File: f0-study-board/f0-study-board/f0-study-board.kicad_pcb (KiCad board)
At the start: 4 copper layers, 47.8 x 19 mm, 26 parts, among them J1 PinHeader-18pin, J2 PinHeader-18pin, J3 USB_B_Micro, J4 SWD, SW1 SW_Reset, U1 STM32F091CBT6, U2 XC6206P332MR, Y1 8MHz

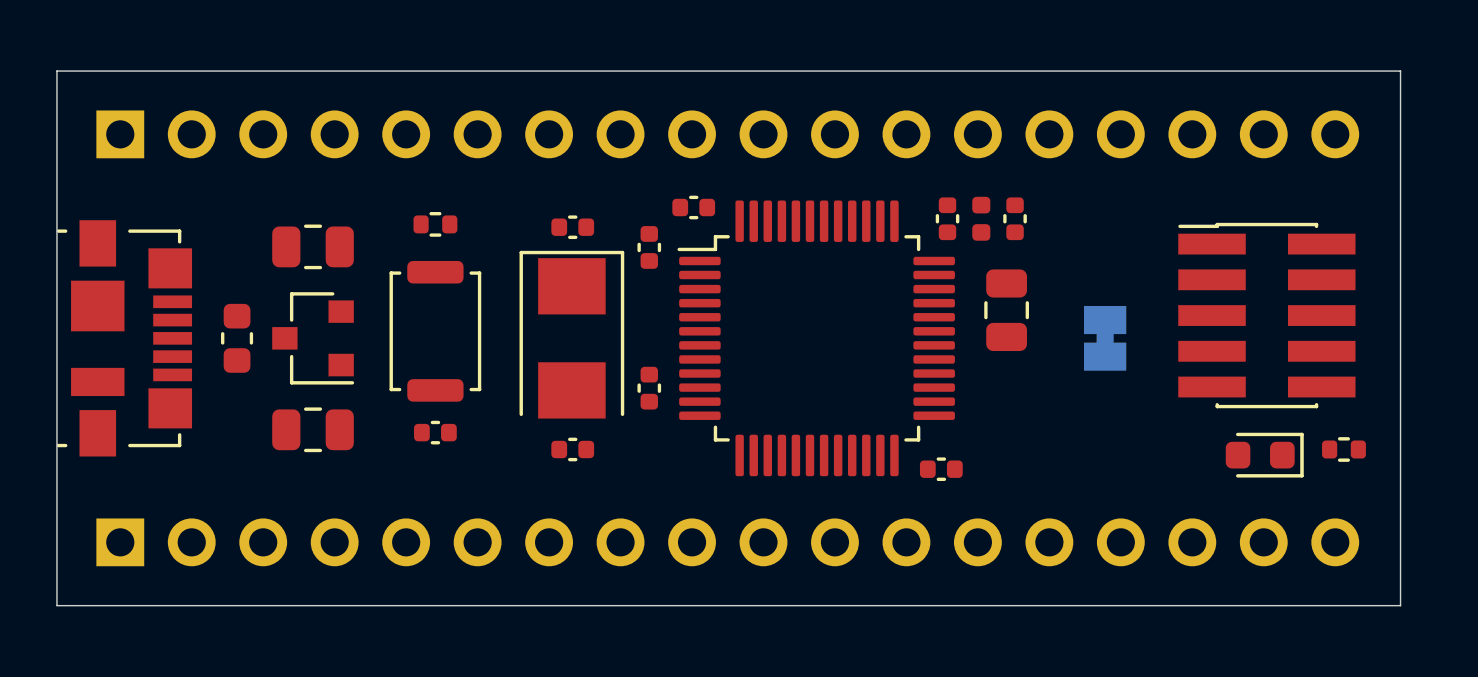
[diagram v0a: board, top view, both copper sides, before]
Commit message: Routed the board, ready for export
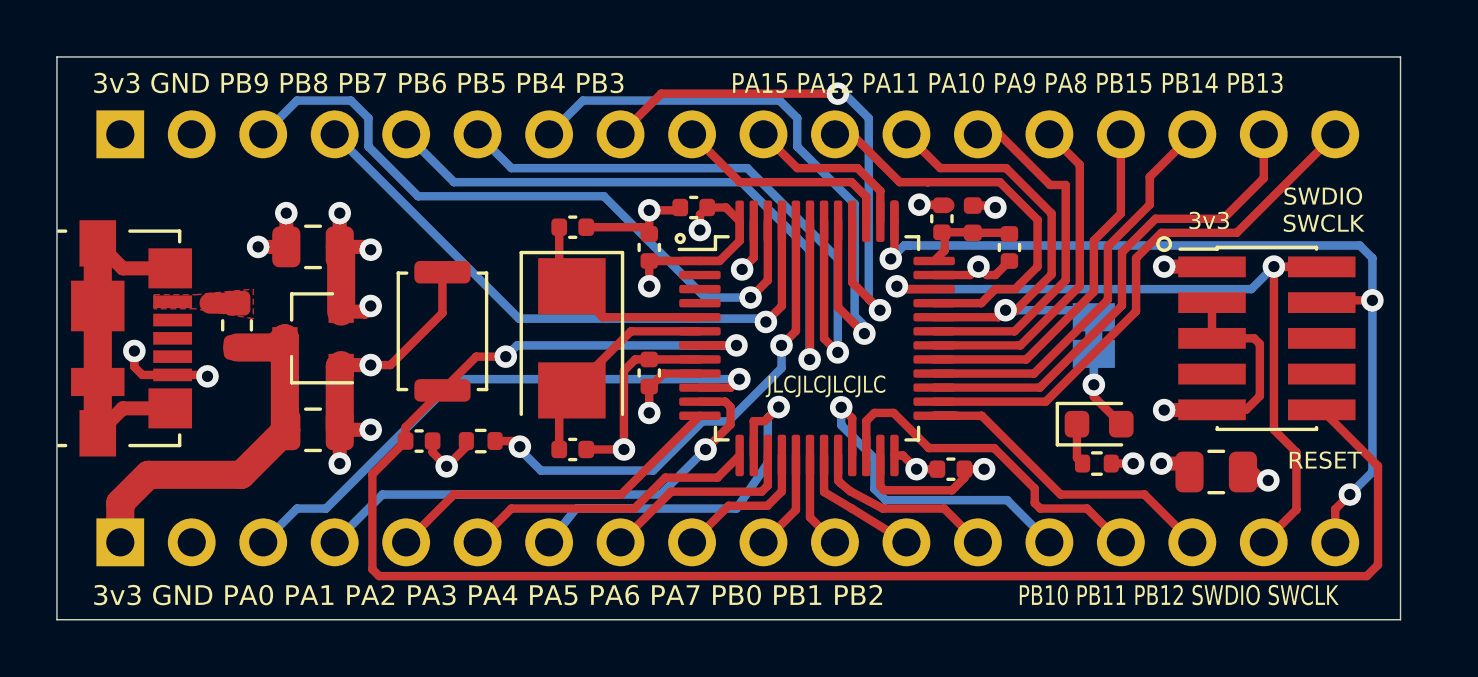
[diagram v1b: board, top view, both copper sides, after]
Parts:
- moved C1 9.41 mm to (138.9, 112.0), turned to 180 degrees
- moved R2 8.79 mm to (134.7, 111.7)
- moved R1 7.87 mm to (112.8, 110.9)
- moved D2 5.83 mm to (134.8, 110.3), turned to 0 degrees
- moved C7 1.04 mm to (131.6, 104.0), turned to 270 degrees
- moved J4 0.81 mm to (140.8, 107.2)
- moved C8 0.65 mm to (110.6, 110.9), turned to 0 degrees
- moved C4 0.54 mm to (118.8, 108.5), turned to 90 degrees
- moved FB1 0.46 mm to (104.2, 106.8)
- moved JP1 0.41 mm to (134.6, 107.2), turned to 270 degrees
- moved C5 0.34 mm to (129.5, 111.9)
- moved L1 0.30 mm to (130.3, 103.0)
- moved SW1 0.25 mm to (111.5, 107.0)
- moved C6 0.20 mm to (129.2, 103.0)
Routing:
- net NRST: track 0.00 -> 62.0 mm, vias 0 -> 2
- net GND: track 0.00 -> 51.8 mm, vias 0 -> 17
- net SWCLK: track 0.00 -> 32.3 mm, vias 0 -> 3
- net SWDIO: track 0.00 -> 29.3 mm, vias 0 -> 2
- net PB7: track 0.00 -> 25.4 mm, vias 0 -> 1
- net PB9: track 0.00 -> 24.3 mm, vias 0 -> 1
- net PB6: track 0.00 -> 22.8 mm, vias 0 -> 1
- net PB5: track 0.00 -> 22.6 mm, vias 0 -> 1
- net PB8: track 0.00 -> 21.7 mm, vias 0 -> 1
- net +3V3: track 0.00 -> 21.6 mm, vias 0 -> 10
- net PA0: track 0.00 -> 20.8 mm, vias 0 -> 1
- net PB4: track 0.00 -> 20.3 mm, vias 0 -> 2
- net PB13: track 0.00 -> 19.3 mm
- net /BOOT0: track 0.00 -> 17.6 mm, vias 0 -> 2
- net PA1: track 0.00 -> 17.6 mm, vias 0 -> 1
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- added copper zone on In2.Cu, net +3V3
- added copper zone on F.Cu, net +5V
- added copper zone on In1.Cu, net GND
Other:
- board size 47.8 x 19 mm -> 47.8 x 20 mm
- board text added: "3v3"
- board text added: "3v3 GND PA0 PA1 PA2 PA3 PA4 PA5 PA6 PA7 PB0 PB1 PB2"
- board text added: "3v3 GND PB9 PB8 PB7 PB6 PB5 PB4 PB3"
- board text added: "JLCJLCJLCJLC"
- board text added: "PA15 PA12 PA11 PA10 PA9 PA8 PB15 PB14 PB13"
- board text added: "PB10 PB11 PB12 SWDIO SWCLK"
- board text added: "RESET"
- board text added: "SWDIO SWCLK"

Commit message: Had to choose another mcu
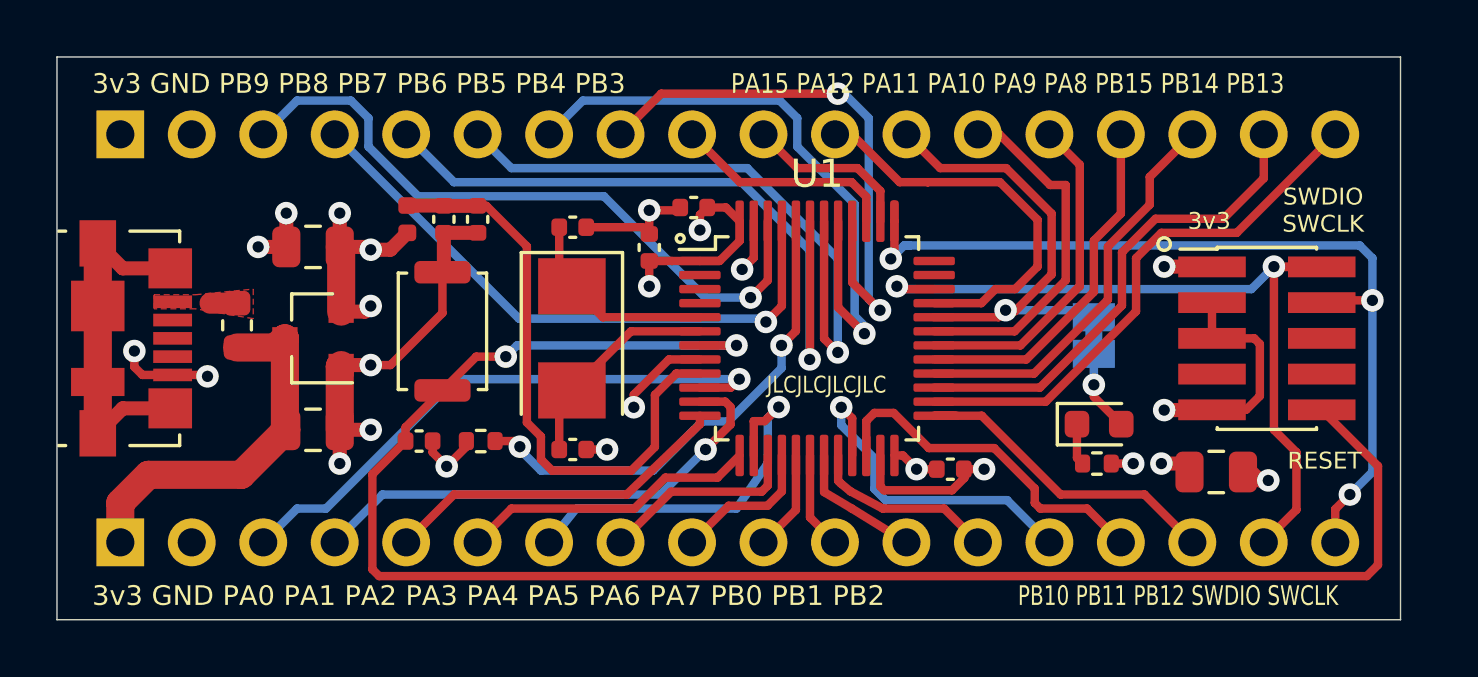
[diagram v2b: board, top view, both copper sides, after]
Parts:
- removed C5: 100n, Capacitor_SMD:C_0402_1005Metric
- U1: value STM32F091CBT6 -> STM32F030C8T6
- moved L1 20.1 mm to (110.2, 103.0), turned to 90 degrees
- moved C7 18.9 mm to (112.7, 103.0)
- moved C6 17.7 mm to (111.5, 103.0), turned to 270 degrees
- moved C4 11.2 mm to (129.5, 111.9), turned to 0 degrees
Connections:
- U1 pad 35: GND -> Net-(U1-Pad35)
- U1 pad 36: +3.3VA -> Net-(U1-Pad36)
- U1 pad 9: +3V3 -> +3.3VA
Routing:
- net +3.3VA: track 3.64 -> 21.0 mm
- net GND: track 51.8 -> 47.2 mm, vias 17 -> 16
- net +3V3: track 21.6 -> 19.3 mm, vias 10 -> 8
